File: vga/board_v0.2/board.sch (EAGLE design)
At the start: 70 parts, among them IC1 AS4C4M16S

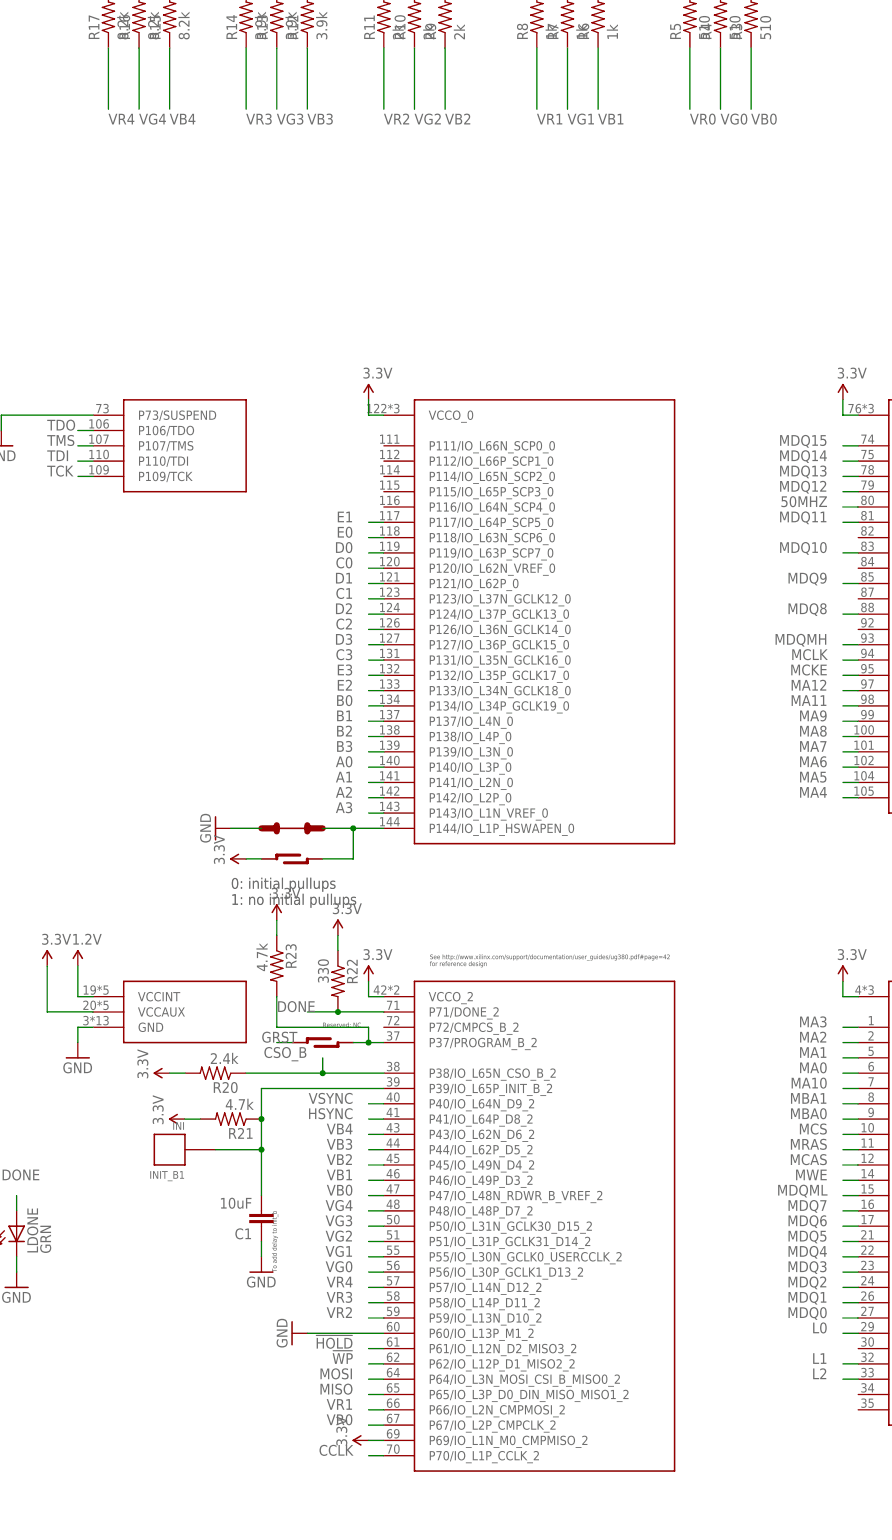
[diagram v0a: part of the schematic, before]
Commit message: Got a very basic vga thing working, though with some issues -- the blue doesn't seem to be working, and I seem to be missing one of the green bits
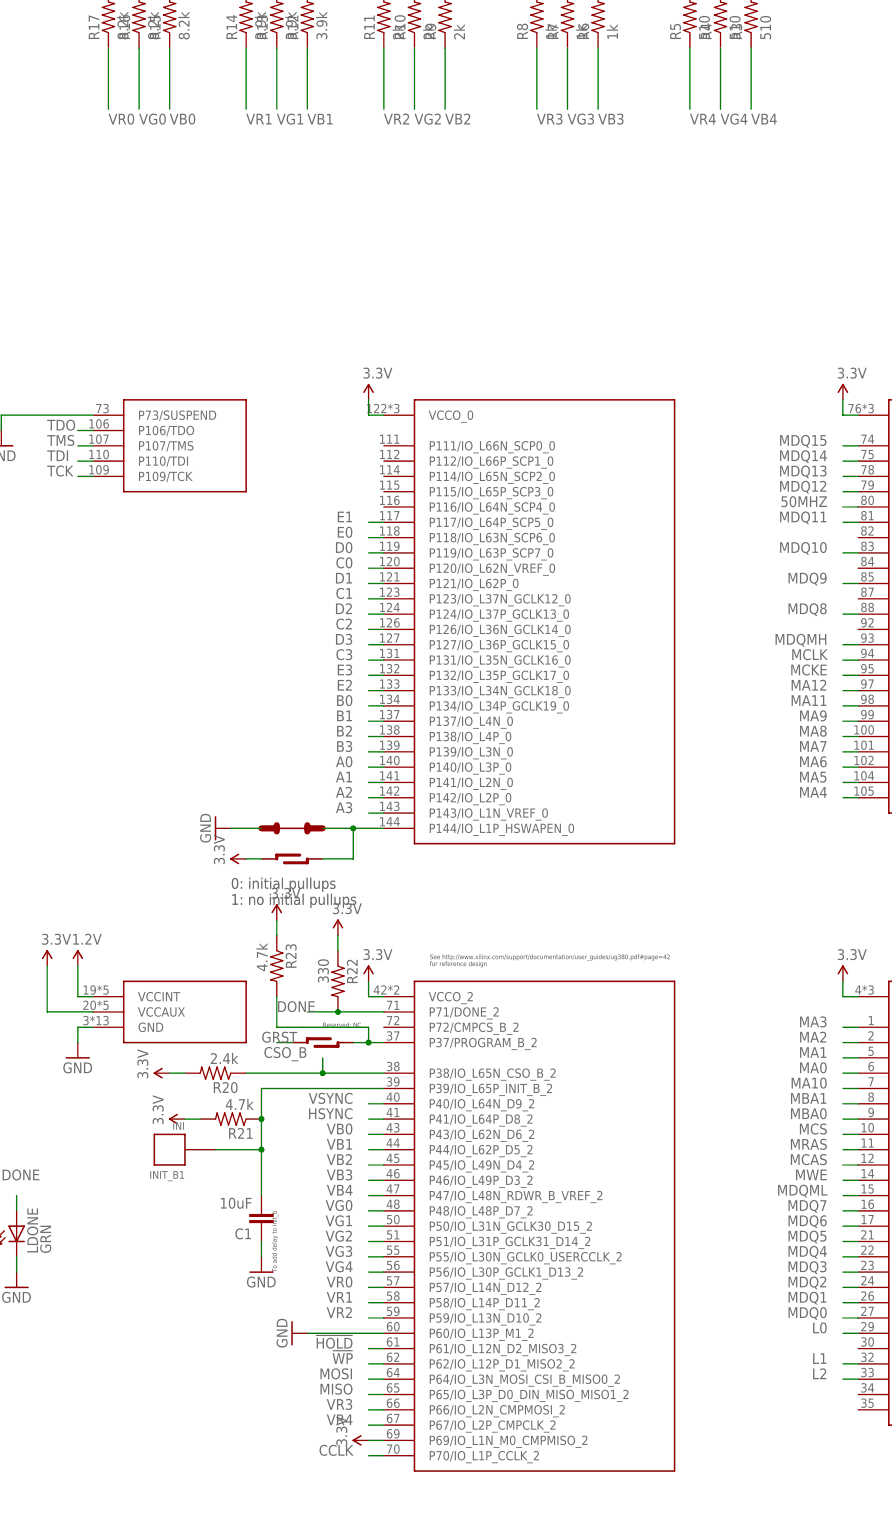
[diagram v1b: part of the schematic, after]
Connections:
- net VB0: now also R15.1, U$9.P43/IO_L62N_D6_2; no longer R3.1, U$9.P47/IO_L48N_RDWR_B_VREF_2
- net VB1: now also R12.1, U$9.P44/IO_L62P_D5_2; no longer R6.1, U$9.P46/IO_L49P_D3_2
- net VB3: now also R6.1, U$9.P46/IO_L49P_D3_2; no longer R12.1, U$9.P44/IO_L62P_D5_2
- net VB4: now also R3.1, U$9.P47/IO_L48N_RDWR_B_VREF_2; no longer R15.1, U$9.P43/IO_L62N_D6_2
- net VG0: now also R16.1, U$9.P48/IO_L48P_D7_2; no longer R4.1, U$9.P56/IO_L30P_GCLK1_D13_2
- net VG1: now also R13.1, U$9.P50/IO_L31N_GCLK30_D15_2; no longer R7.1, U$9.P55/IO_L30N_GCLK0_USERCCLK_2
- net VG3: now also R7.1, U$9.P55/IO_L30N_GCLK0_USERCCLK_2; no longer R13.1, U$9.P50/IO_L31N_GCLK30_D15_2
- net VG4: now also R4.1, U$9.P56/IO_L30P_GCLK1_D13_2; no longer R16.1, U$9.P48/IO_L48P_D7_2
- net VR0: now also R17.1, U$9.P57/IO_L14N_D12_2; no longer R5.1, U$9.P67/IO_L2P_CMPCLK_2
- net VR1: now also R14.1, U$9.P58/IO_L14P_D11_2; no longer R8.1, U$9.P66/IO_L2N_CMPMOSI_2
- net VR3: now also R8.1, U$9.P66/IO_L2N_CMPMOSI_2; no longer R14.1, U$9.P58/IO_L14P_D11_2
- net VR4: now also R5.1, U$9.P67/IO_L2P_CMPCLK_2; no longer R17.1, U$9.P57/IO_L14N_D12_2
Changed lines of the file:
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@@
 <?xml version="1.0" encoding="utf-8"?>
 <!DOCTYPE eagle SYSTEM "eagle.dtd">
-<eagle version="6.4">
+<eagle version="6.5.0">
 <drawing>
 <settings>
@@
 <grid distance="0.1" unitdist="inch" unit="inch" style="lines" multiple="1" display="no" altdistance="0.01" altunitdist="inch" altunit="inch"/>
 <layers>
-<layer number="1" name="Top" color="4" fill="1" visible="yes" active="no"/>
-<layer number="2" name="Route2" color="1" fill="3" visible="yes" active="no"/>
-<layer number="3" name="Route3" color="4" fill="3" visible="yes" active="no"/>
-<layer number="4" name="Route4" color="1" fill="4" visible="yes" active="no"/>
-<layer number="5" name="Route5" color="4" fill="4" visible="yes" active="no"/>
-<layer number="6" name="Route6" color="1" fill="8" visible="yes" active="no"/>
-<layer number="7" name="Route7" color="4" fill="8" visible="yes" active="no"/>
-<layer number="8" name="Route8" color="1" fill="2" visible="yes" active="no"/>
-<layer number="9" name="Route9" color="4" fill="2" visible="yes" active="no"/>
-<layer number="10" name="Route10" color="1" fill="7" visible="yes" active="no"/>
-<layer number="11" name="Route11" color="4" fill="7" visible="yes" active="no"/>
-<layer number="12" name="Route12" color="1" fill="5" visible="yes" active="no"/>
-<layer number="13" name="Route13" color="4" fill="5" visible="yes" active="no"/>
-<layer number="14" name="Route14" color="1" fill="6" visible="yes" active="no"/>
-<layer number="15" name="Route15" color="4" fill="6" visible="yes" active="no"/>
-<layer number="16" name="Bottom" color="1" fill="1" visible="yes" active="no"/>
-<layer number="17" name="Pads" color="2" fill="1" visible="yes" active="no"/>
-<layer number="18" name="Vias" color="2" fill="1" visible="yes" active="no"/>
-<layer number="19" name="Unrouted" color="6" fill="1" visible="yes" active="no"/>
-<layer number="20" name="Dimension" color="15" fill="1" visible="yes" active="no"/>
-<layer number="21" name="tPlace" color="16" fill="1" visible="yes" active="no"/>
-<layer number="22" name="bPlace" color="14" fill="1" visible="yes" active="no"/>
-<layer number="23" name="tOrigins" color="15" fill="1" visible="yes" active="no"/>
-<layer number="24" name="bOrigins" color="15" fill="1" visible="yes" active="no"/>
-<layer number="25" name="tNames" color="7" fill="1" visible="yes" active="no"/>
-<layer number="26" name="bNames" color="7" fill="1" visible="yes" active="no"/>
-<layer number="27" name="tValues" color="7" fill="1" visible="yes" active="no"/>
-<layer number="28" name="bValues" color="7" fill="1" visible="yes" active="no"/>
+<layer number="1" name="Top" color="4" fill="1" visible="no" active="no"/>
+<layer number="2" name="Route2" color="1" fill="3" visible="no" active="no"/>
+<layer number="3" name="Route3" color="4" fill="3" visible="no" active="no"/>
+<layer number="4" name="Route4" color="1" fill="4" visible="no" active="no"/>
+<layer number="5" name="Route5" color="4" fill="4" visible="no" active="no"/>
+<layer number="6" name="Route6" color="1" fill="8" visible="no" active="no"/>
+<layer number="7" name="Route7" color="4" fill="8" visible="no" active="no"/>
+<layer number="8" name="Route8" color="1" fill="2" visible="no" active="no"/>
+<layer number="9" name="Route9" color="4" fill="2" visible="no" active="no"/>
+<layer number="10" name="Route10" color="1" fill="7" visible="no" active="no"/>
+<layer number="11" name="Route11" color="4" fill="7" visible="no" active="no"/>
+<layer number="12" name="Route12" color="1" fill="5" visible="no" active="no"/>
+<layer number="13" name="Route13" color="4" fill="5" visible="no" active="no"/>
+<layer number="14" name="Route14" color="1" fill="6" visible="no" active="no"/>
+<layer number="15" name="Route15" color="4" fill="6" visible="no" active="no"/>
+<layer number="16" name="Bottom" color="1" fill="1" visible="no" active="no"/>
+<layer number="17" name="Pads" color="2" fill="1" visible="no" active="no"/>
+<layer number="18" name="Vias" color="2" fill="1" visible="no" active="no"/>
+<layer number="19" name="Unrouted" color="6" fill="1" visible="no" active="no"/>
+<layer number="20" name="Dimension" color="15" fill="1" visible="no" active="no"/>
+<layer number="21" name="tPlace" color="16" fill="1" visible="no" active="no"/>
+<layer number="22" name="bPlace" color="14" fill="1" visible="no" active="no"/>
+<layer number="23" name="tOrigins" color="15" fill="1" visible="no" active="no"/>
+<layer number="24" name="bOrigins" color="15" fill="1" visible="no" active="no"/>
+<layer number="25" name="tNames" color="7" fill="1" visible="no" active="no"/>
+<layer number="26" name="bNames" color="7" fill="1" visible="no" active="no"/>
+<layer number="27" name="tValues" color="7" fill="1" visible="no" active="no"/>
+<layer number="28" name="bValues" color="7" fill="1" visible="no" active="no"/>
 <layer number="29" name="tStop" color="7" fill="3" visible="no" active="no"/>
 <layer number="30" name="bStop" color="7" fill="6" visible="no" active="no"/>
@@
 <layer number="35" name="tGlue" color="7" fill="4" visible="no" active="no"/>
 <layer number="36" name="bGlue" color="7" fill="5" visible="no" active="no"/>
-<layer number="37" name="tTest" color="7" fill="1" visible="yes" active="no"/>
-<layer number="38" name="bTest" color="7" fill="1" visible="yes" active="no"/>
+<layer number="37" name="tTest" color="7" fill="1" visible="no" active="no"/>
+<layer number="38" name="bTest" color="7" fill="1" visible="no" active="no"/>
 <layer number="39" name="tKeepout" color="4" fill="11" visible="no" active="no"/>
 <layer number="40" name="bKeepout" color="1" fill="11" visible="no" active="no"/>
@@
 <layer number="44" name="Drills" color="7" fill="1" visible="no" active="no"/>
 <layer number="45" name="Holes" color="7" fill="1" visible="no" active="no"/>
-<layer number="46" name="Milling" color="3" fill="1" visible="yes" active="no"/>
-<layer number="47" name="Measures" color="7" fill="1" visible="yes" active="no"/>
-<layer number="48" name="Document" color="7" fill="1" visible="yes" active="no"/>
-<layer number="49" name="Reference" color="7" fill="1" visible="yes" active="no"/>
-<layer number="50" name="dxf" color="7" fill="1" visible="yes" active="no"/>
-<layer number="51" name="tDocu" color="6" fill="1" visible="yes" active="no"/>
-<layer number="52" name="bDocu" color="7" fill="1" visible="yes" active="no"/>
-<layer number="53" name="tGND_GNDA" color="7" fill="9" visible="yes" active="no"/>
-<layer number="54" name="bGND_GNDA" color="1" fill="9" visible="yes" active="no"/>
-<layer number="56" name="wert" color="7" fill="1" visible="yes" active="no"/>
+<layer number="46" name="Milling" color="3" fill="1" visible="no" active="no"/>
+<layer number="47" name="Measures" color="7" fill="1" visible="no" active="no"/>
+<layer number="48" name="Document" color="7" fill="1" visible="no" active="no"/>
+<layer number="49" name="Reference" color="7" fill="1" visible="no" active="no"/>
+<layer number="50" name="dxf" color="7" fill="1" visible="no" active="no"/>
+<layer number="51" name="tDocu" color="6" fill="1" visible="no" active="no"/>
+<layer number="52" name="bDocu" color="7" fill="1" visible="no" active="no"/>
+<layer number="53" name="tGND_GNDA" color="7" fill="9" visible="no" active="no"/>
+<layer number="54" name="bGND_GNDA" color="1" fill="9" visible="no" active="no"/>
+<layer number="56" name="wert" color="7" fill="1" visible="no" active="no"/>
 <layer number="91" name="Nets" color="2" fill="1" visible="yes" active="yes"/>
 <layer number="92" name="Busses" color="1" fill="1" visible="yes" active="yes"/>
@@
 </segment>
 </net>
-<net name="VB0" class="0">
+<net name="VB4" class="0">
 <segment>
 <wire x1="-25.4" y1="261.62" x2="-25.4" y2="251.46" width="0.1524" layer="91"/>
@@
 </segment>
 </net>
-<net name="VG0" class="0">
+<net name="VG4" class="0">
 <segment>
 <wire x1="-30.48" y1="261.62" x2="-30.48" y2="251.46" width="0.1524" layer="91"/>
@@
 </segment>
 </net>
-<net name="VR0" class="0">
+<net name="VR4" class="0">
 <segment>
 <wire x1="-35.56" y1="261.62" x2="-35.56" y2="251.46" width="0.1524" layer="91"/>
@@
 </segment>
 </net>
-<net name="VB1" class="0">
+<net name="VB3" class="0">
 <segment>
 <wire x1="-50.8" y1="261.62" x2="-50.8" y2="251.46" width="0.1524" layer="91"/>
@@
 </segment>
 </net>
-<net name="VG1" class="0">
+<net name="VG3" class="0">
 <segment>
 <wire x1="-55.88" y1="261.62" x2="-55.88" y2="251.46" width="0.1524" layer="91"/>
@@
 </segment>
 </net>
-<net name="VR1" class="0">
+<net name="VR3" class="0">
 <segment>
 <wire x1="-60.96" y1="261.62" x2="-60.96" y2="251.46" width="0.1524" layer="91"/>
@@
 </segment>
 </net>
-<net name="VB3" class="0">
+<net name="VB1" class="0">
 <segment>
 <wire x1="-99.06" y1="261.62" x2="-99.06" y2="251.46" width="0.1524" layer="91"/>
@@
 </segment>
 </net>
-<net name="VG3" class="0">
+<net name="VG1" class="0">
 <segment>
 <wire x1="-104.14" y1="261.62" x2="-104.14" y2="251.46" width="0.1524" layer="91"/>
@@
 </segment>
 </net>
-<net name="VR3" class="0">
+<net name="VR1" class="0">
 <segment>
 <wire x1="-109.22" y1="261.62" x2="-109.22" y2="251.46" width="0.1524" layer="91"/>
@@
 </segment>
 </net>
-<net name="VB4" class="0">
+<net name="VB0" class="0">
 <segment>
 <wire x1="-121.92" y1="261.62" x2="-121.92" y2="251.46" width="0.1524" layer="91"/>
@@
 </segment>
 </net>
-<net name="VG4" class="0">
+<net name="VG0" class="0">
 <segment>
 <wire x1="-127" y1="261.62" x2="-127" y2="251.46" width="0.1524" layer="91"/>
@@
 </segment>
 </net>
-<net name="VR4" class="0">
+<net name="VR0" class="0">
 <segment>
 <wire x1="-132.08" y1="261.62" x2="-132.08" y2="251.46" width="0.1524" layer="91"/>

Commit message: Working on vga board v0.3
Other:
- note added: "Planned revisions: - better reset logic, either from button or MB - sdram pads are on the short side - connect the oscillator to a GCLK pin - add buffers to the jtag pins - use a supported flash part"
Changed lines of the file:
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@@
 <?xml version="1.0" encoding="utf-8"?>
 <!DOCTYPE eagle SYSTEM "eagle.dtd">
-<eagle version="6.5.0">
+<eagle version="6.4">
 <drawing>
 <settings>
@@
 for reference design</text>
 <text x="-104.14" y="58.42" size="0.762" layer="97" rot="R90">To add delay to init_b</text>
+<text x="96.52" y="119.38" size="3.556" layer="97">Planned revisions:
+- better reset logic, either from button or MB
+- sdram pads are on the short side
+- connect the oscillator to a GCLK pin
+- add buffers to the jtag pins
+- use a supported flash part</text>
 </plain>
 <instances>
